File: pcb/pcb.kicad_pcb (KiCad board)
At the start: 2 copper layers, 10 parts, among them J1 Audio Jack, SW1 SW_Push, U1 LCD-016N002L

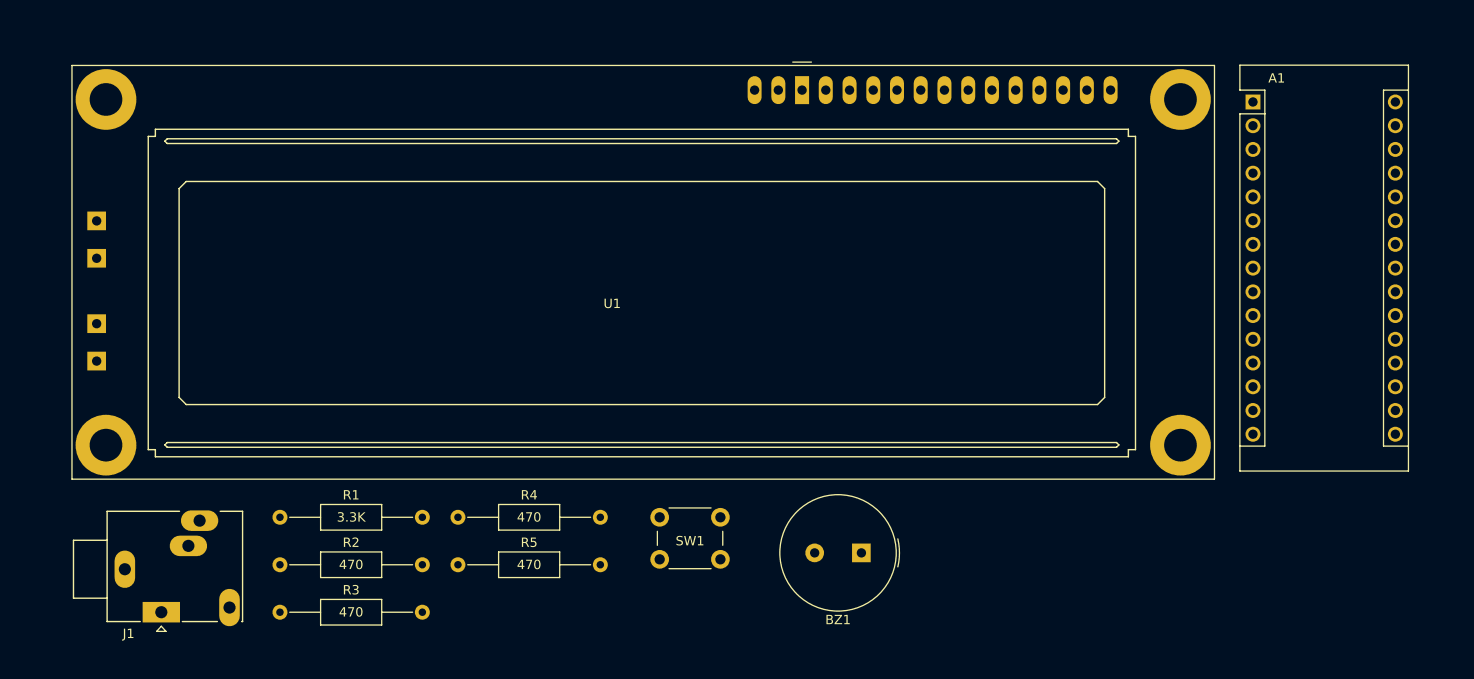
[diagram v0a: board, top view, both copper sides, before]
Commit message: Finished pcb wiring
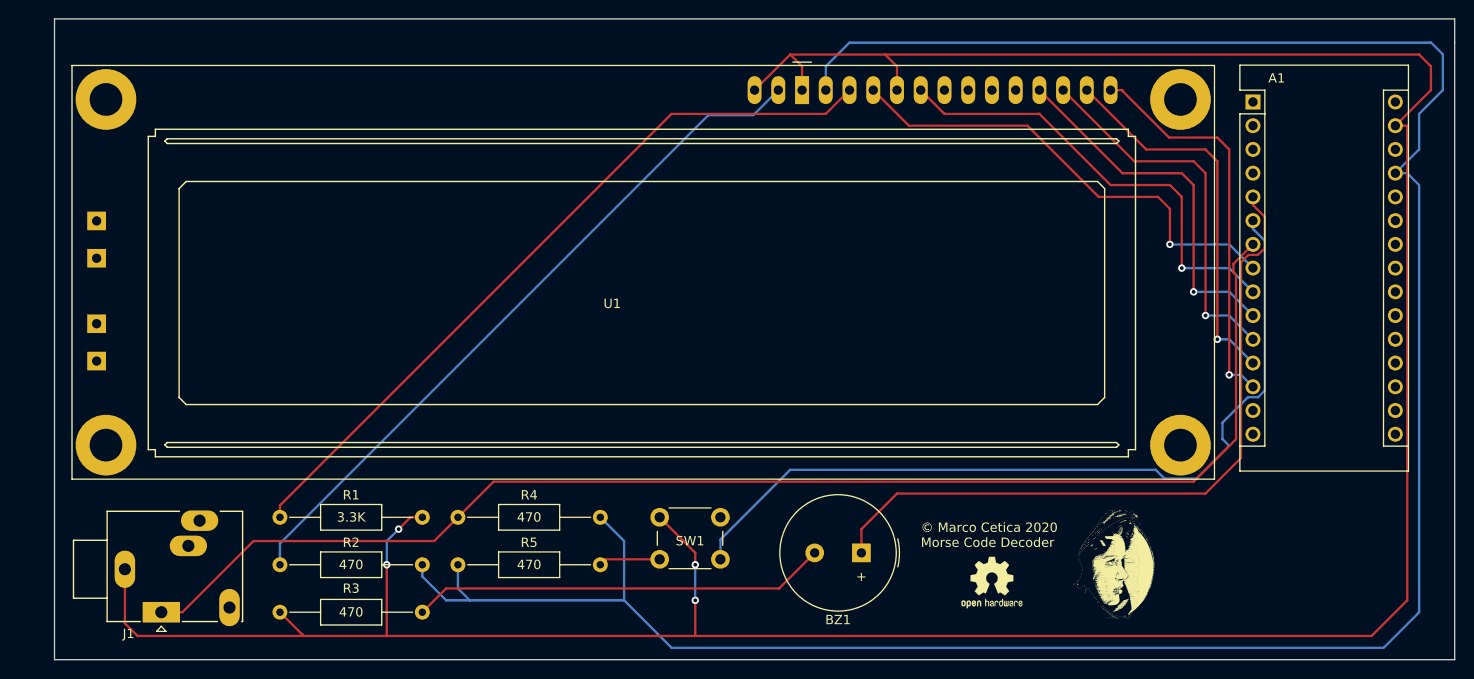
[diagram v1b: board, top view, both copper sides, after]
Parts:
- added G***: LOGO, pcb:avatar, F.Cu at (194.9, 127.0)
- added REF**: OSHW-Logo2_7.3x6mm_SilkScreen, Symbol:OSHW-Logo2_7.3x6mm_SilkScreen, F.Cu at (181.6, 128.9)
- moved R3 15.2 mm to (120.7, 132.1), turned to 180 degrees
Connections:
- net KEY_NEG renamed GND
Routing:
- net GND: track 0.00 -> 321.2 mm, vias 0 -> 4
- net +5V: track 0.00 -> 260.7 mm
- net KEY_POS: track 0.00 -> 144.5 mm
- net Net-(A1-Pad6): track 0.00 -> 95.5 mm
- net Net-(R1-Pad1): track 0.00 -> 80.6 mm
- net Net-(A1-Pad5): track 0.00 -> 76.5 mm
- net Net-(R2-Pad1): track 0.00 -> 75.7 mm
- net Net-(A1-Pad8): track 0.00 -> 50.8 mm, vias 0 -> 1
- net Net-(A1-Pad9): track 0.00 -> 49.0 mm, vias 0 -> 1
- net Net-(BZ1-Pad2): track 0.00 -> 44.6 mm
- net Net-(A1-Pad13): track 0.00 -> 42.6 mm, vias 0 -> 1
- net Net-(A1-Pad12): track 0.00 -> 41.0 mm, vias 0 -> 1
- net Net-(A1-Pad11): track 0.00 -> 40.3 mm, vias 0 -> 1
- net Net-(A1-Pad10): track 0.00 -> 39.6 mm, vias 0 -> 1
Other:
- board outline added: 149.9 x 68.6 mm
- board text added: "+"
- board text added: "© Marco Cetica 2020 Morse Code Decoder"

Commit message: Redesigned pcb due to a bug
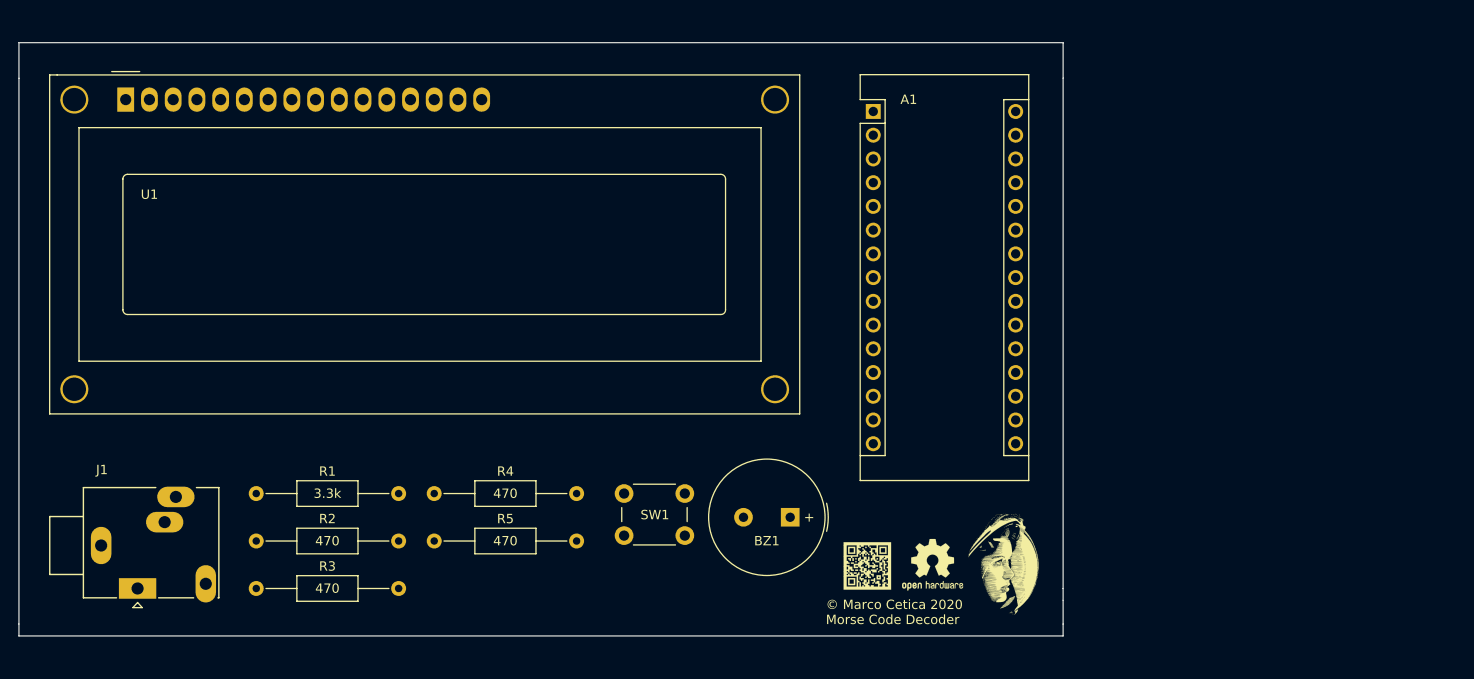
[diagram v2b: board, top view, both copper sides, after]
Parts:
- added G***: LOGO, pcb:qrcode, F.Cu at (168.3, 127.1)
- U1: footprint Display:LCD-016N002L -> Display:WC1602A
- moved U1 72.4 mm to (88.9, 77.2)
- moved A1 40.7 mm to (168.9, 78.5)
- moved R3 18.0 mm to (102.9, 129.5), turned to 0 degrees
- moved G*** 12.1 mm to (182.9, 127.0)
- moved BZ1 8.52 mm to (160.0, 121.9)
- moved REF** 6.63 mm to (175.3, 127.0)
- moved SW1 4.58 mm to (142.2, 119.4)
- moved J1 3.59 mm to (90.2, 129.5)
- moved R1 3.59 mm to (102.9, 119.4)
- moved R2 3.59 mm to (102.9, 124.5)
- moved R4 3.59 mm to (121.9, 119.4)
- moved R5 3.59 mm to (121.9, 124.5)
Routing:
- net GND: track 321.2 -> 0.00 mm, vias 4 -> 0
- net +5V: track 260.7 -> 0.00 mm
- net KEY_POS: track 144.5 -> 0.00 mm
- net Net-(A1-Pad6): track 95.5 -> 0.00 mm
- net Net-(R1-Pad1): track 80.6 -> 0.00 mm
- net Net-(A1-Pad5): track 76.5 -> 0.00 mm
- net Net-(R2-Pad1): track 75.7 -> 0.00 mm
- net Net-(A1-Pad8): track 50.8 -> 0.00 mm, vias 1 -> 0
- net Net-(A1-Pad9): track 49.0 -> 0.00 mm, vias 1 -> 0
- net Net-(BZ1-Pad2): track 44.6 -> 0.00 mm
- net Net-(A1-Pad13): track 42.6 -> 0.00 mm, vias 1 -> 0
- net Net-(A1-Pad12): track 41.0 -> 0.00 mm, vias 1 -> 0
- net Net-(A1-Pad11): track 40.3 -> 0.00 mm, vias 1 -> 0
- net Net-(A1-Pad10): track 39.6 -> 0.00 mm, vias 1 -> 0
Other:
- board size 149.9 x 68.6 mm -> 111.8 x 63.5 mm
- board text added: "3.3k"
- board text removed: "3.3K"

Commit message: rewired pcb
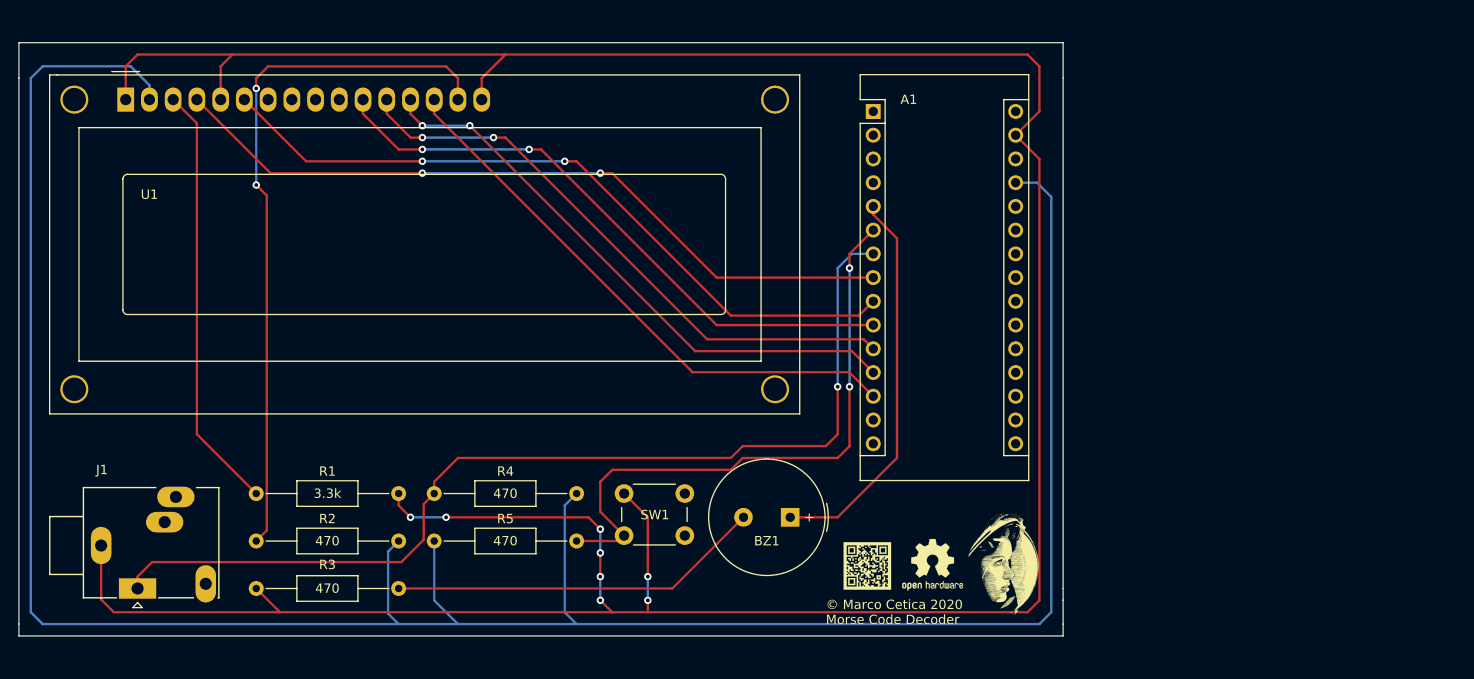
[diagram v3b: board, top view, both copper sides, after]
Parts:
- moved R3 15.2 mm to (118.1, 129.5), turned to 180 degrees
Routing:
- net GND: track 0.00 -> 330.8 mm, vias 0 -> 8
- net +5V: track 0.00 -> 266.7 mm
- net KEY_POS: track 0.00 -> 107.7 mm, vias 0 -> 1
- net Net-(A1-Pad8): track 0.00 -> 80.3 mm, vias 0 -> 2
- net Net-(A1-Pad9): track 0.00 -> 77.5 mm, vias 0 -> 2
- net Net-(R2-Pad1): track 0.00 -> 75.4 mm, vias 0 -> 2
- net Net-(A1-Pad10): track 0.00 -> 65.5 mm, vias 0 -> 2
- net Net-(A1-Pad6): track 0.00 -> 64.6 mm, vias 0 -> 2
- net Net-(A1-Pad11): track 0.00 -> 64.0 mm, vias 0 -> 2
- net Net-(A1-Pad12): track 0.00 -> 62.5 mm, vias 0 -> 2
- net Net-(A1-Pad13): track 0.00 -> 61.0 mm
- net Net-(R1-Pad1): track 0.00 -> 45.8 mm
- net Net-(A1-Pad5): track 0.00 -> 42.0 mm
- net Net-(BZ1-Pad2): track 0.00 -> 40.1 mm

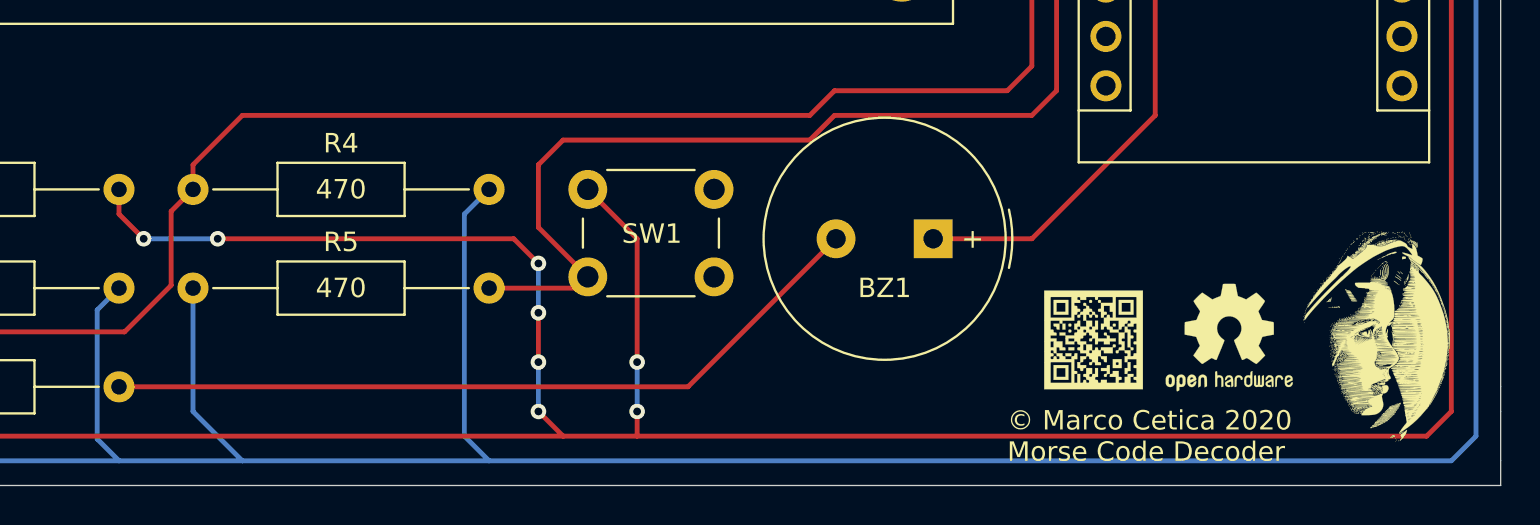
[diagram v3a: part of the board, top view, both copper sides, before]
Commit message: Update pin numbers
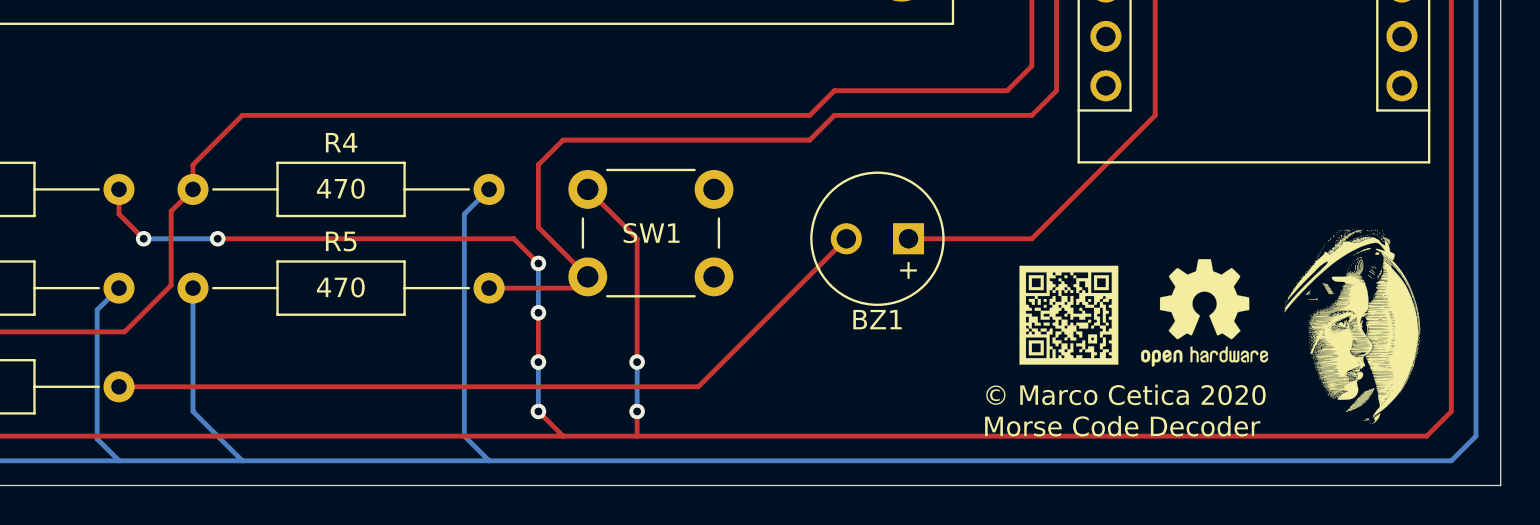
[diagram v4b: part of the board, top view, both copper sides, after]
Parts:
- BZ1: footprint Buzzer_Beeper:Buzzer_TDK_PS1240P02BT_D12.2mm_H6.5mm -> Buzzer_Beeper:MagneticBuzzer_Kingstate_KCG0601
- moved G*** 1.80 mm to (167.0, 125.9)
- moved REF** 1.80 mm to (174.0, 125.7)
- moved G*** 1.37 mm to (181.6, 126.5)
- moved BZ1 1.27 mm to (158.8, 121.9)
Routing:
- net Net-(A1-Pad5): track 42.0 -> 43.3 mm
- net Net-(BZ1-Pad2): track 40.1 -> 40.6 mm
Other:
- board text removed: "+"

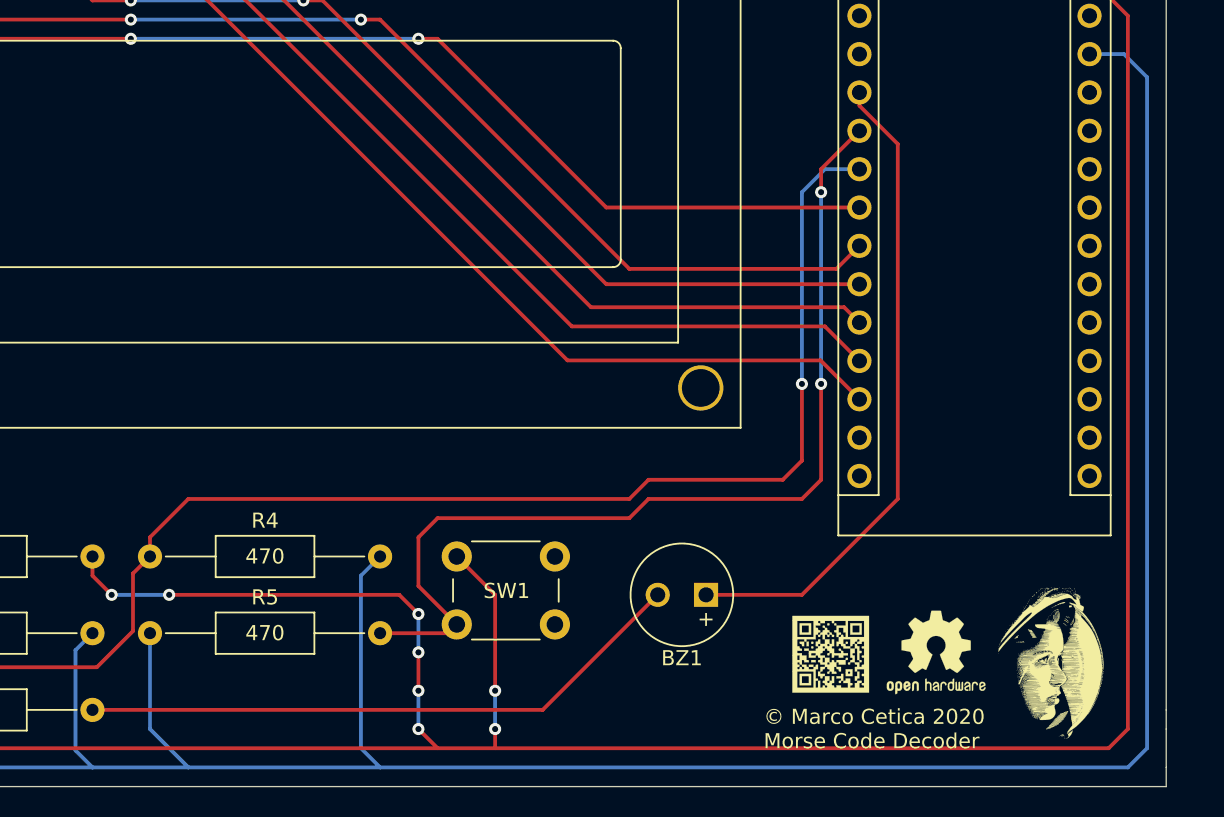
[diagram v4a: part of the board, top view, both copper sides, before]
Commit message: Updated a footprint
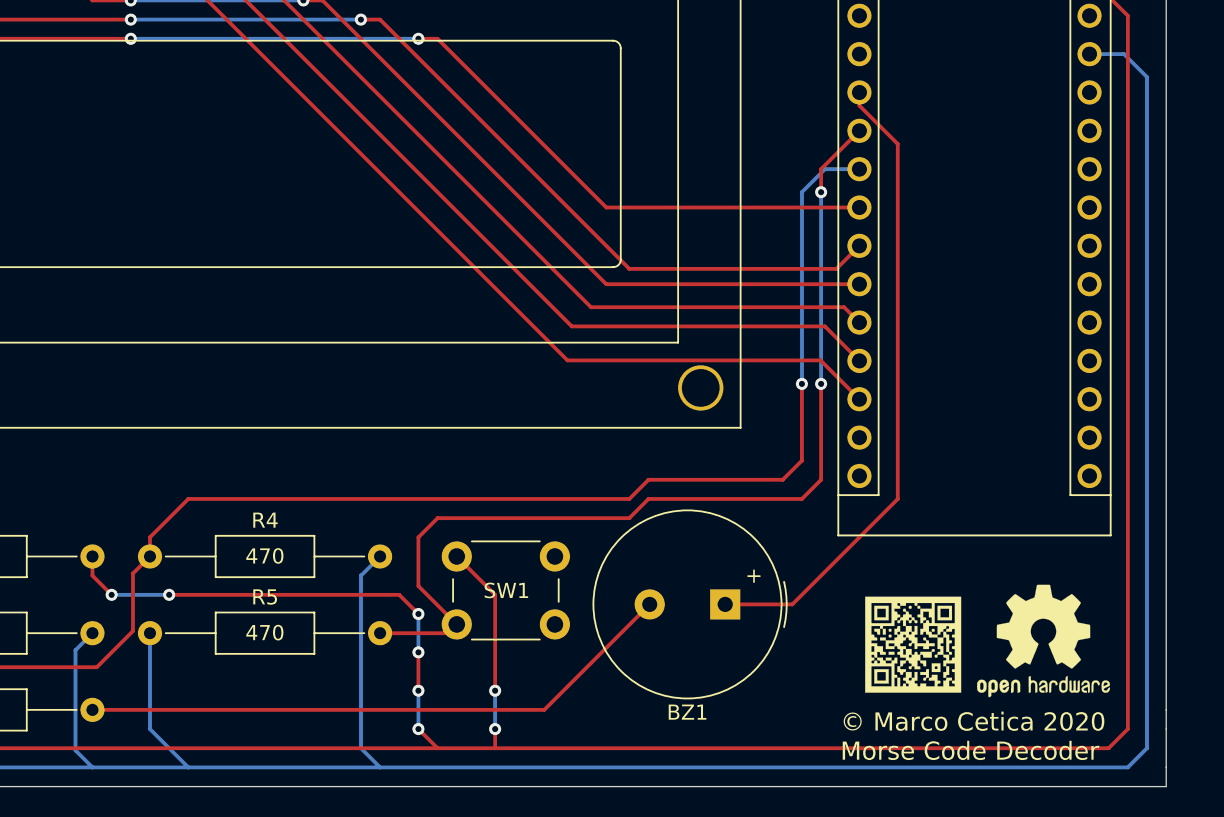
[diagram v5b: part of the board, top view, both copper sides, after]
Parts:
- removed the G*** at (181.6, 126.5)
- removed the REF** at (174.0, 125.7)
- added REF**: OSHW-Logo2_9.8x8mm_SilkScreen, Symbol:OSHW-Logo2_9.8x8mm_SilkScreen, F.Cu at (181.1, 125.0)
- BZ1: footprint Buzzer_Beeper:MagneticBuzzer_Kingstate_KCG0601 -> Buzzer_Beeper:Buzzer_TDK_PS1240P02BT_D12.2mm_H6.5mm
- moved G*** 5.50 mm to (172.5, 125.2)
- moved BZ1 1.42 mm to (160.0, 122.6)
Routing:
- net Net-(A1-Pad5): track 43.3 -> 42.3 mm
- net Net-(BZ1-Pad2): track 40.6 -> 39.8 mm
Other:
- board text added: "+"
